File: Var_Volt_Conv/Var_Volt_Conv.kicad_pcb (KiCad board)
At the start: 6 copper layers, 114 x 86 mm, 98 parts, among them J101 Jack-DC, J102 Screw_Terminal_01x02, J103 Screw_Terminal_01x02, J201 Conn_01x05, Q101 AO3416, Q102 IRFML8244TRPBF, Q103 IRFML8244TRPBF, Q104 AO3407, Q105 AO3407, Q106 AO3407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

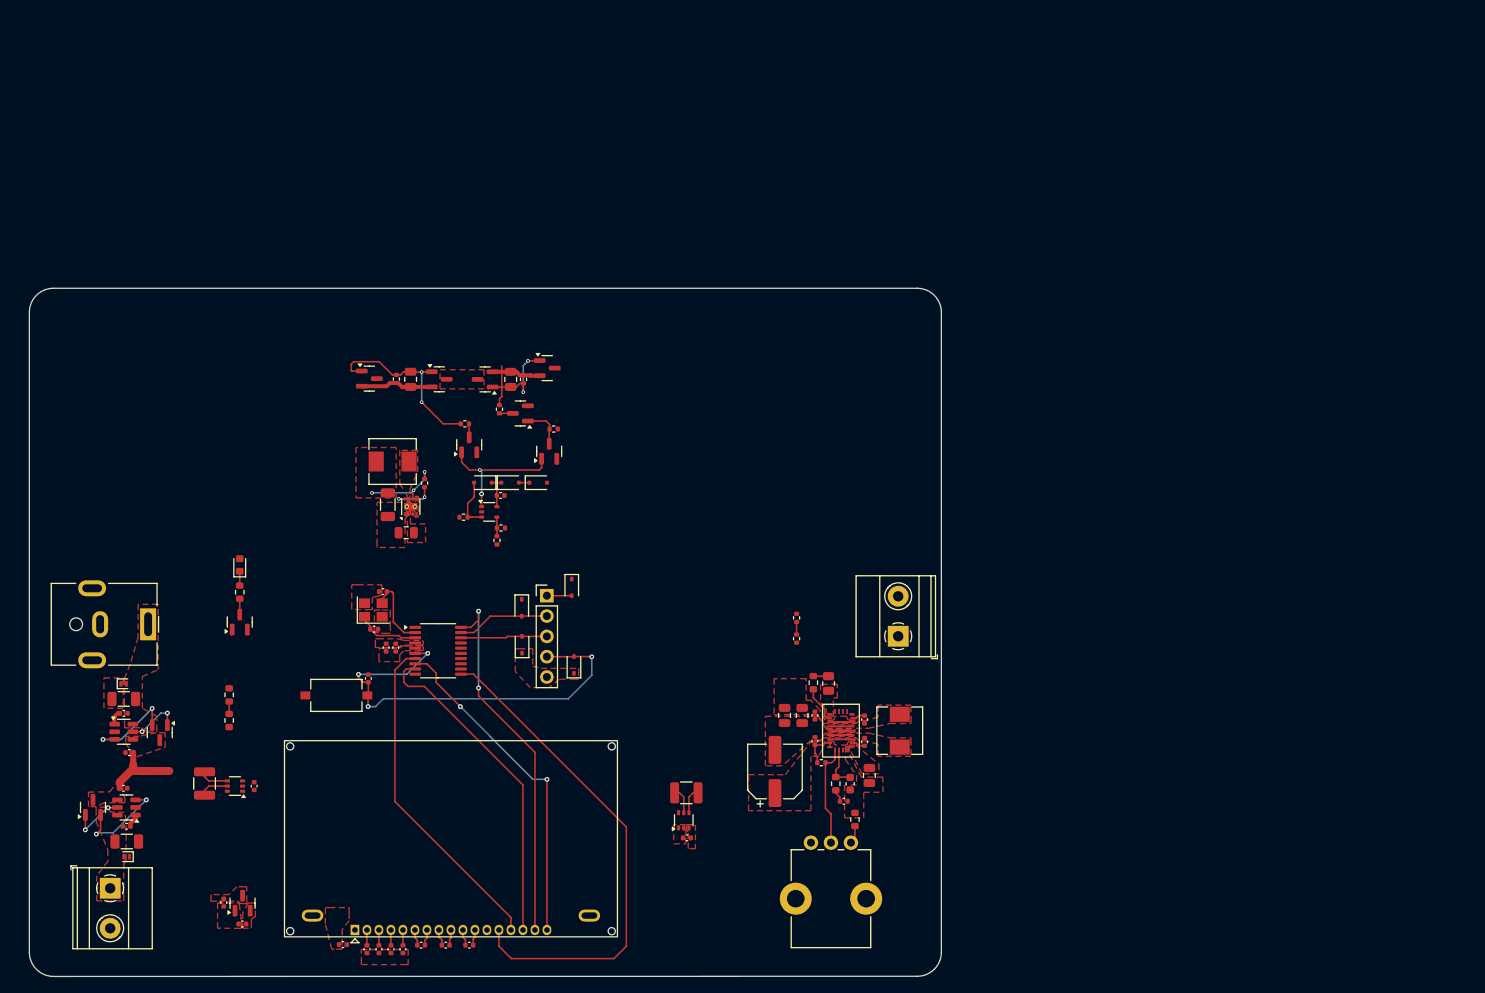
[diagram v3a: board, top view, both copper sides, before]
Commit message: Finish organizing sub-circuits, and input voltage sensor sensing System_voltage_input_A instead of B
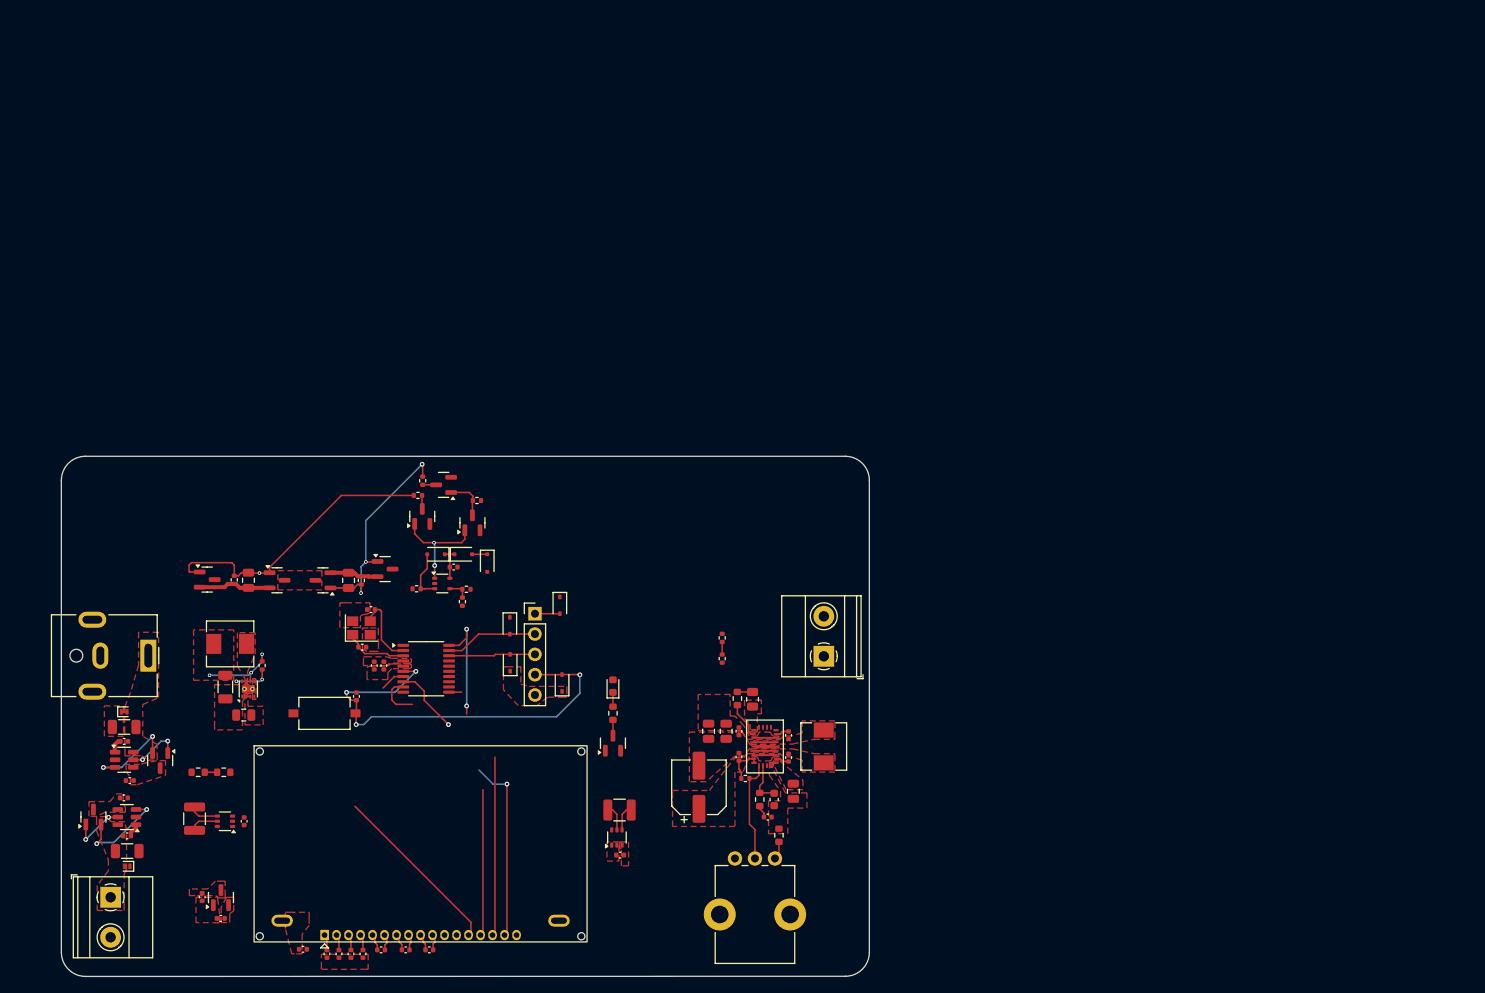
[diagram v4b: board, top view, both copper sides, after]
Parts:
- moved D106 49.0 mm to (93.0, 103.7)
- moved Q110 49.0 mm to (93.0, 110.9)
- moved R113 49.0 mm to (93.0, 107.1)
- moved C110 32.3 mm to (59.9, 90.5)
- moved Q105 32.3 mm to (51.0, 90.5)
- moved C108 32.3 mm to (47.4, 90.5)
- moved Q107 32.3 mm to (56.7, 90.5)
- moved R105 32.3 mm to (45.6, 90.5)
- moved R107 32.3 mm to (61.5, 90.5)
- moved Q106 32.3 mm to (64.5, 89.1)
- moved Q104 32.3 mm to (42.2, 90.4)
- moved L101 30.5 mm to (45.1, 98.5)
- moved R109 30.5 mm to (49.1, 101.2)
- moved C109 30.5 mm to (46.8, 107.3)
- moved C111 30.5 mm to (44.5, 103.8)
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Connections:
- R401 pad 1: SYSTEM_POWER_B -> SYSTEM_POWER_A
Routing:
- net SPI_MOSI: track 62.7 -> 23.6 mm
- net /CHIP_SELECT: track 42.0 -> 8.54 mm, vias 2 -> 1
- net SPI_CLK: track 41.6 -> 21.2 mm
- net /[1] Power/BUCK_PPM_GATE: track 23.0 -> 36.4 mm, vias 2 -> 1
- net REGISTER_SELECT: track 41.2 -> 27.9 mm
- net SYSTEM_POWER_A: track 15.5 -> 3.69 mm
- net /[1] Power/ST_PPM_GATE: track 15.8 -> 27.5 mm, vias 2 -> 3
- net /RESET: track 46.4 -> 37.3 mm, vias 2 -> 3
- net /[1] Power/COMP_OUT: track 17.6 -> 13.8 mm
- net /[1] Power/ST_3V3_Diode: track 1.30 -> 1.90 mm
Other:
- board size 114 x 86 mm -> 101 x 65 mm
- board text added: "3V"
- board text added: "In(I) Se"
- board text added: "In(V) Se"
- board text added: "P. Ind."
- board text removed: "3V Power"
- board text removed: "Input (I) Sensor"
- board text removed: "Input (V) Sensor"
- board text removed: "Power Ind."

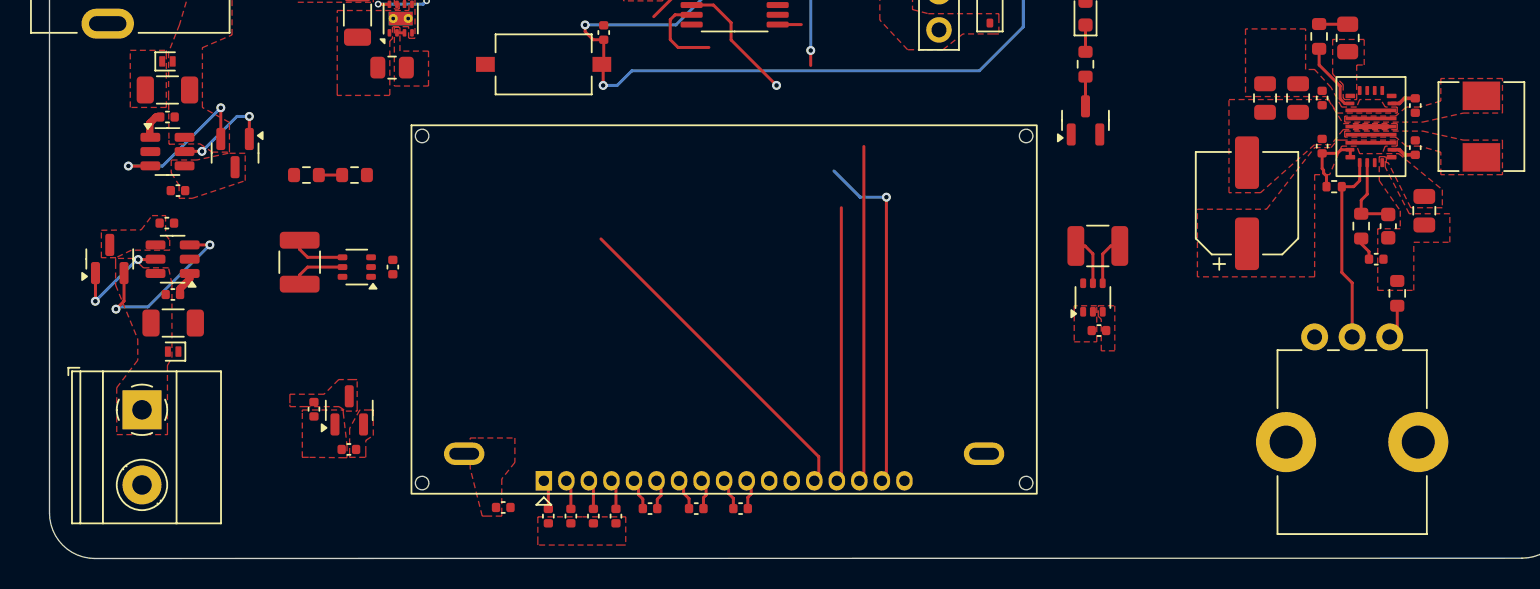
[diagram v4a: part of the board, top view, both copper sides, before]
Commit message: Add Power, digital and analog grounds
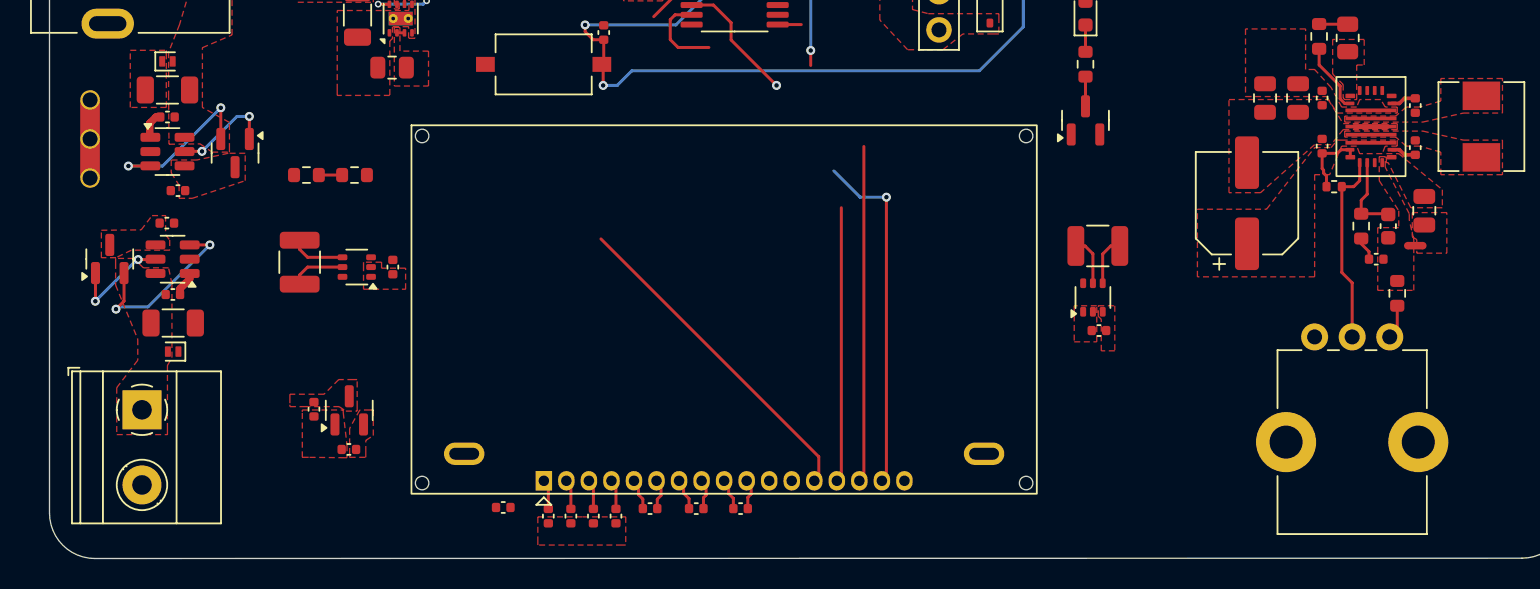
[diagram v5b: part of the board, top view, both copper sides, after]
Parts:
- added NT101: NetTie_3, NetTie:NetTie-3_THT_Pad1.0mm, F.Cu at (26.7, 114.7)
- added NT102: NetTie_2, NetTie:NetTie-2_SMD_Pad0.5mm, F.Cu at (114.9, 119.2)
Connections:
- C101 pad 2: GND -> GNDPWR
- C102 pad 2: GND -> GNDPWR
- C103 pad 2: GND -> GNDPWR
- C106 pad 2: GND -> GNDPWR
- C107 pad 2: GND -> GNDPWR
- C109 pad 2: GND -> GNDPWR
- C111 pad 2: GND -> GNDPWR
- C112 pad 2: GND -> GNDPWR
- C113 pad 2: GND -> GNDPWR
- C114 pad 2: GND -> GNDPWR
- C115 pad 2: GND -> GNDPWR
- C118 pad 2: GND -> GNDPWR
- C119 pad 2: GND -> GNDA
- C120 pad 2: GND -> GNDPWR
- C121 pad 2: GND -> GNDA
- C122 pad 2: GND -> GNDPWR
- C123 pad 2: GND -> GNDPWR
- C201 pad 2: GND -> GNDD
- C202 pad 2: GND -> GNDD
- C203 pad 1: GND -> GNDD
- C204 pad 1: GND -> GNDD
- C205 pad 2: GND -> GNDD
- C301 pad 1: GND -> GNDD
- C302 pad 1: GND -> GNDD
- C303 pad 1: GND -> GNDD
- C304 pad 1: GND -> GNDD
- C305 pad 1: GND -> GNDD
- C306 pad 1: GND -> GNDD
- C401 pad 2: GND -> GNDA
- C402 pad 2: GND -> GNDA
- D101 pad 1: GND -> GNDPWR
- D102 pad 1: GND -> GNDPWR
- D201 pad 1: GND -> GNDD
- D202 pad 1: GND -> GNDD
- D203 pad 1: GND -> GNDD
- D204 pad 1: GND -> GNDD
- J101 pad 2: GND -> GNDPWR
- J102 pad 2: GND -> GNDPWR
- J103 pad 2: GND -> GNDPWR
- J201 pad 5: GND -> GNDD
- Q101 pad 2: GND -> GNDPWR
- Q108 pad 2: GND -> GNDPWR
- Q109 pad 2: GND -> GNDPWR
- Q110 pad 2: GND -> GNDPWR
- R103 pad 2: GND -> GNDPWR
- R112 pad 2: GND -> GNDA
- R117 pad 2: GND -> GNDA
- R402 pad 2: GND -> GNDPWR
- R404 pad 2: GND -> GNDPWR
- SW201 pad 1: GND -> GNDD
- U101 pad 2: GND -> GNDPWR
- U102 pad 2: GND -> GNDPWR
- U103 pad 2: GND -> GNDPWR
- U104 pad 1: GND -> GNDPWR
- U104 pad 4: GND -> GNDPWR
- U104 pad 5: GND -> GNDPWR
- U104 pad 9: GND -> GNDPWR
- U105 pad 17: GND -> GNDA
- U105 pad 5: GND -> GNDA
- U105 pad 9: GND -> GNDPWR
- U106 pad 1: GND -> GNDPWR
- U201 pad 5: GND -> GNDD
- U301 pad 11: GND -> GNDD
- U301 pad 19: GND -> GNDD
- U401 pad 1: GND -> GNDA
- U401 pad 2: GND -> GNDA
- U402 pad 1: GND -> GNDA
- U402 pad 2: GND -> GNDA
- Y201 pad 2: GND -> GNDD
- Y201 pad 4: GND -> GNDD
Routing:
- net GND: track 1.99 -> 0.00 mm
- net /[3] Display/LVOUT: track 2.03 -> 4.02 mm
- added copper zone on F.Cu, net GNDA
- added copper zone on F.Cu, net GNDD
- added copper zone on F.Cu, net GNDPWR

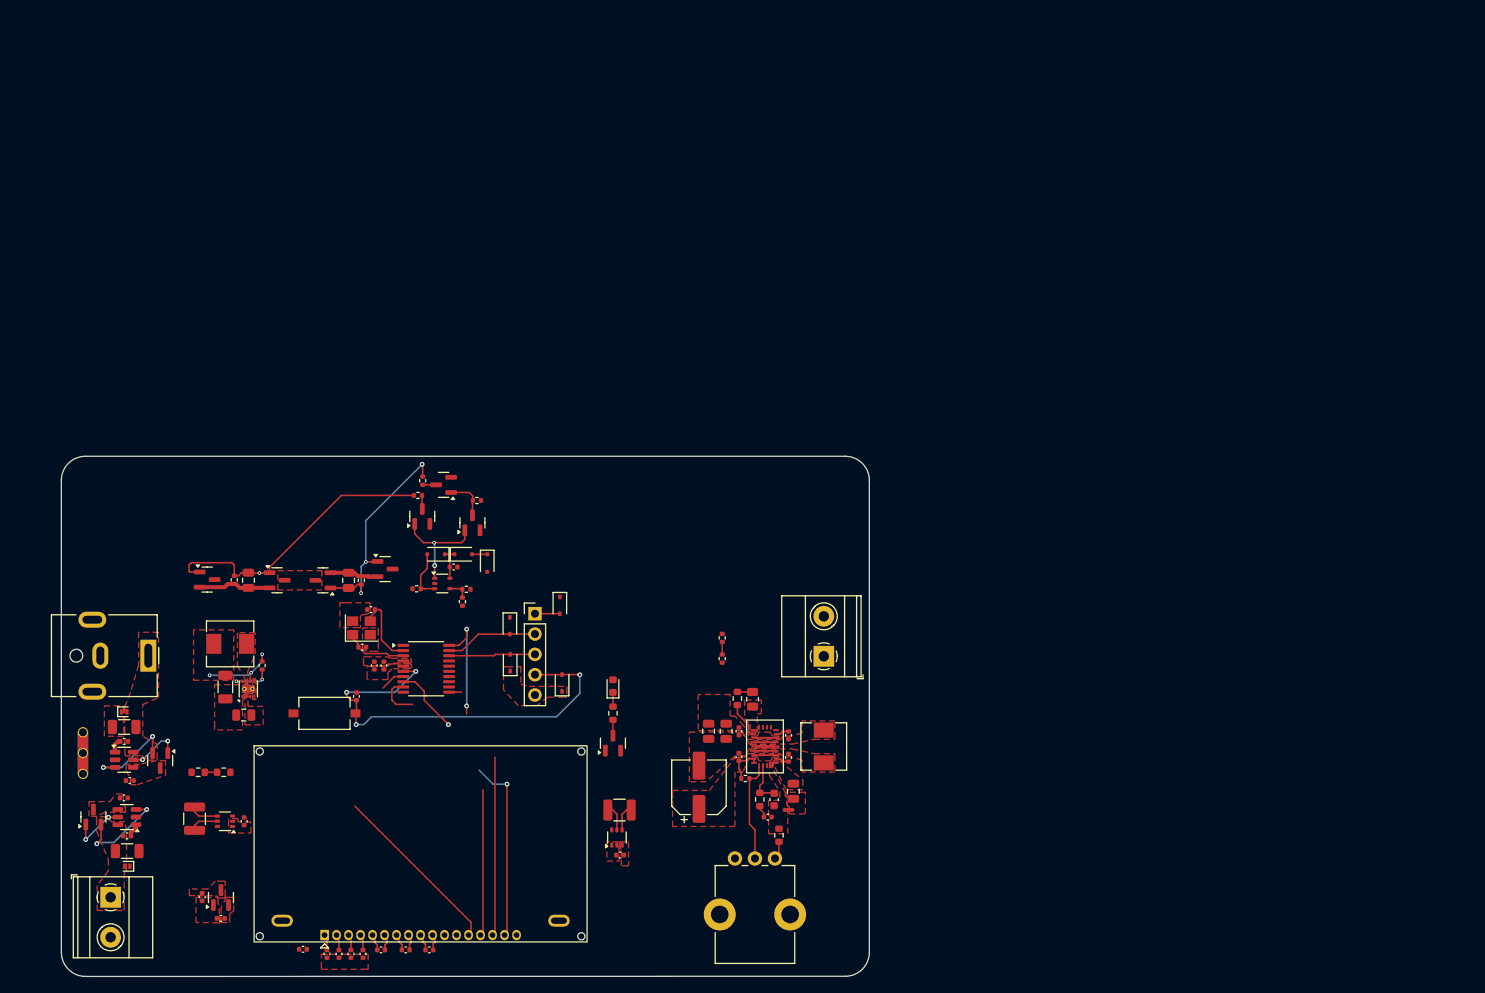
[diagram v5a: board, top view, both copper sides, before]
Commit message: Finish tracing all non-power related nets, changed uC pins for Chip Select, Register Select, Reset, Output Voltage sensing, input current sensing and output voltage sensing
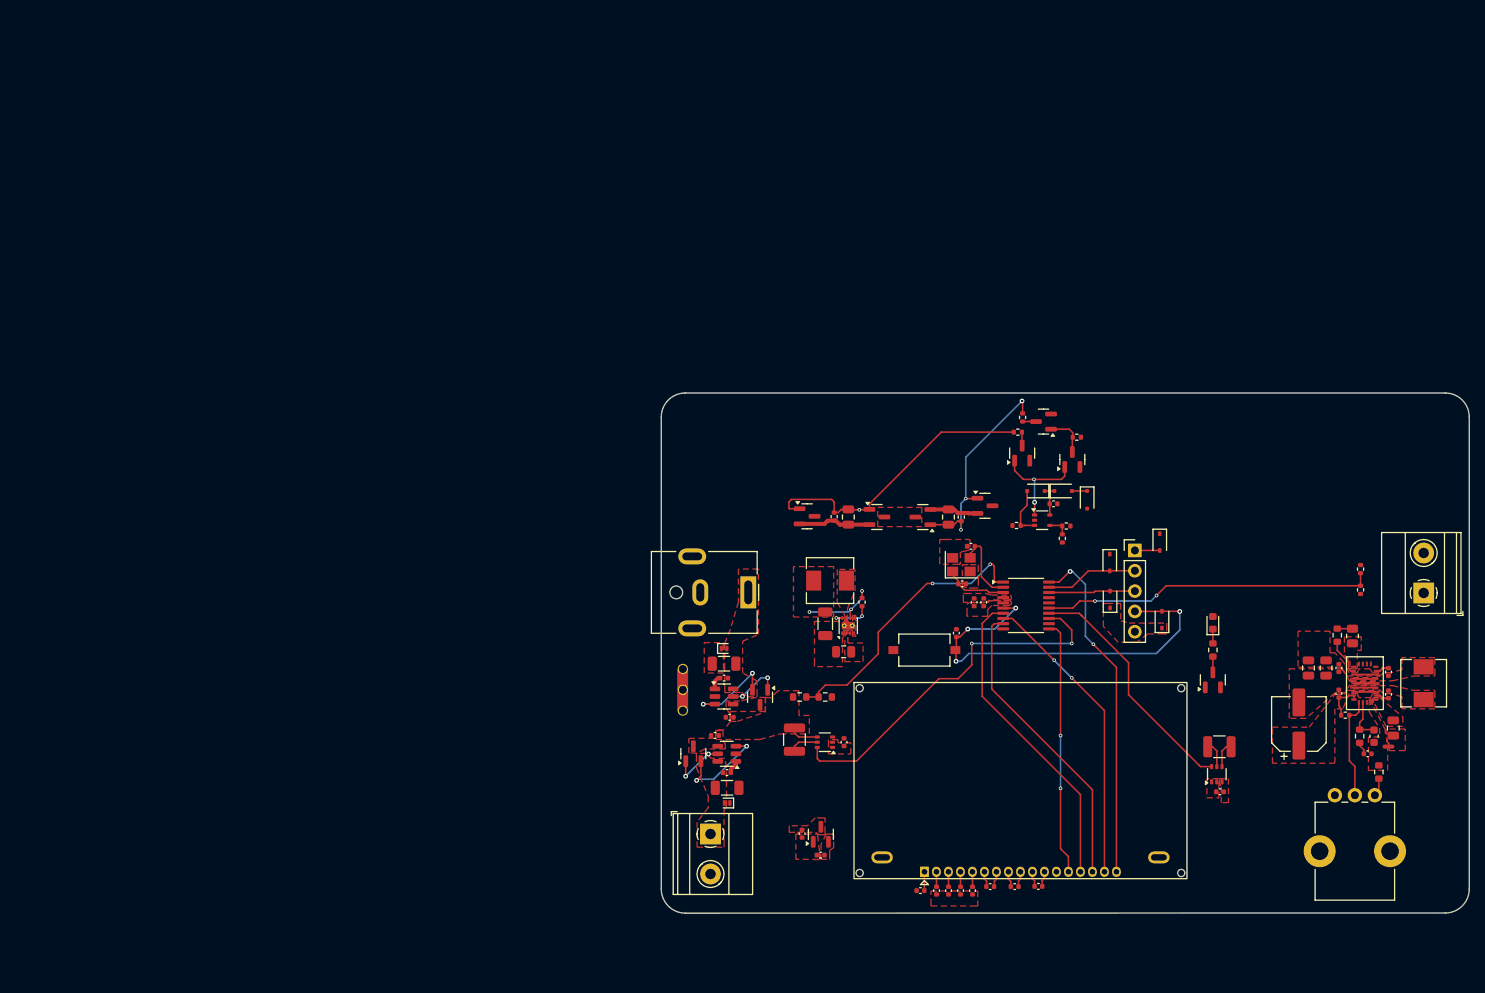
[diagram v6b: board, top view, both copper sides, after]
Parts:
- moved R403 80.3 mm to (186.4, 91.7)
- moved R404 80.3 mm to (186.4, 89.1)
- moved C302 77.5 mm to (131.4, 129.3)
- moved C303 76.6 mm to (133.4, 129.3)
- moved C304 76.6 mm to (134.9, 129.3)
- moved C305 76.6 mm to (136.4, 129.3)
- moved C306 76.6 mm to (137.9, 129.3)
- moved C301 76.5 mm to (146.1, 128.8)
- moved C307 76.5 mm to (140.1, 128.8)
- moved C308 76.5 mm to (143.2, 128.8)
- moved R401 75.8 mm to (116.3, 105.1)
- moved R402 75.8 mm to (119.5, 105.1)
- moved C401 75.6 mm to (121.8, 110.7)
- moved R106 75.6 mm to (115.6, 110.4)
- moved U401 75.6 mm to (119.4, 110.7)
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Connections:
- U201 pad 13: S-OUTPUT_CURRENT -> S-INPUT_CURRENT
- U201 pad 14: S-OUTPUT_VOLTAGE -> S-OUTPUT_CURRENT
- U201 pad 15: S-INPUT_CURRENT -> S-OUTPUT_VOLTAGE
- U201 pad 20: /RESET -> /CHIP_SELECT
- U201 pad 8: /CHIP_SELECT -> /RESET
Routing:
- net S-INPUT_CURRENT: track 0.00 -> 46.2 mm, vias 0 -> 2
- net S-OUTPUT_VOLTAGE: track 1.57 -> 41.7 mm, vias 0 -> 2
- net /CHIP_SELECT: track 8.54 -> 43.3 mm, vias 1 -> 2
- net S-INPUT_VOLTAGE: track 1.55 -> 35.4 mm, vias 0 -> 2
- net S-OUTPUT_CURRENT: track 0.00 -> 30.8 mm
- net SPI_CLK: track 21.2 -> 39.7 mm
- net REGISTER_SELECT: track 27.9 -> 37.5 mm
- net SPI_MOSI: track 23.6 -> 31.9 mm, vias 0 -> 2
- net /[2] Microcontroller/NRST: track 53.9 -> 51.2 mm
- net /[3] Display/LV0: track 0.00 -> 2.36 mm
- net /[3] Display/LVOUT: track 4.02 -> 1.93 mm
- net GNDD: track 0.00 -> 1.94 mm
- net /RESET: track 37.3 -> 37.6 mm, vias 3 -> 2
- removed copper zone on F.Cu, net GND
